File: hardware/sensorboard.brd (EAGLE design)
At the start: 21.5 x 85 mm, 29 parts, among them U3 QRE1113, U4 QRE1113, U5 QRE1113, U6 QRE1113, U7 QRE1113, U8 QRE1113, U9 QRE1113

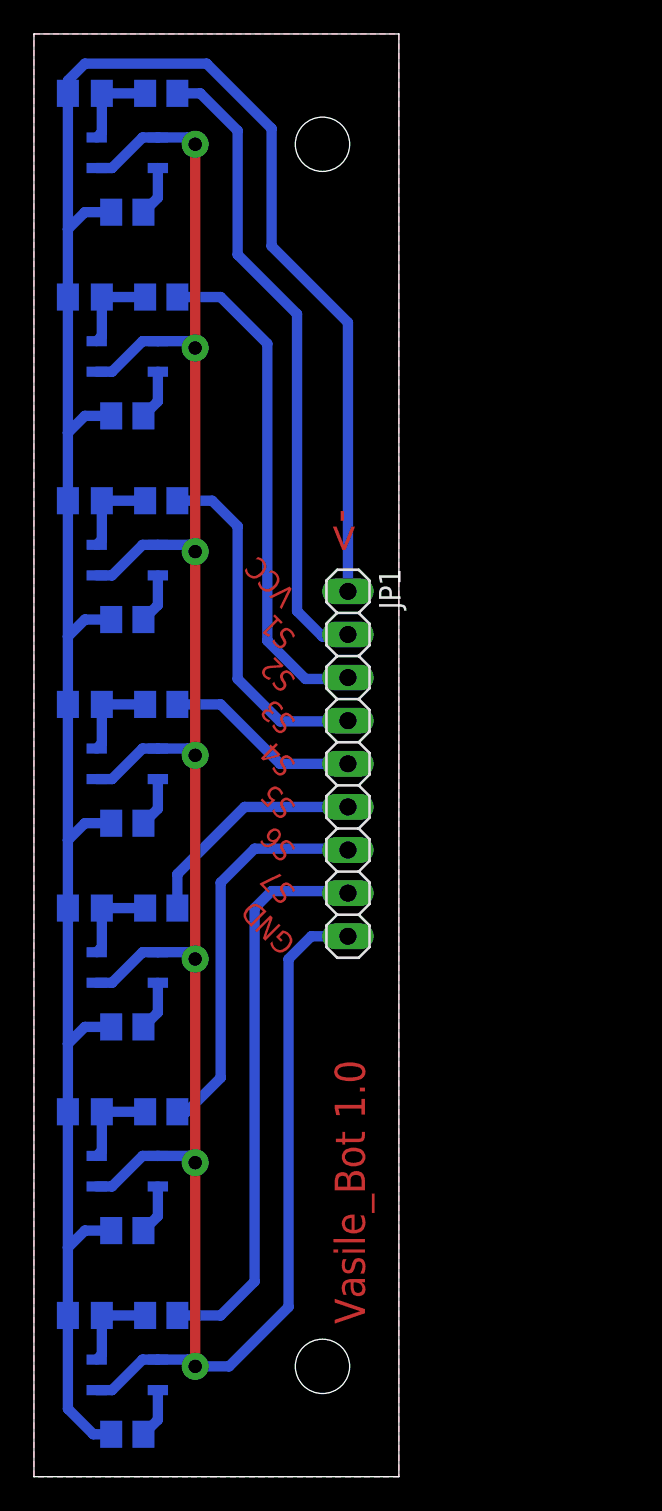
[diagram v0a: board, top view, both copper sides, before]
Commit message: Added ball caster. Added halls for ball caster. Fixed mounting halls.
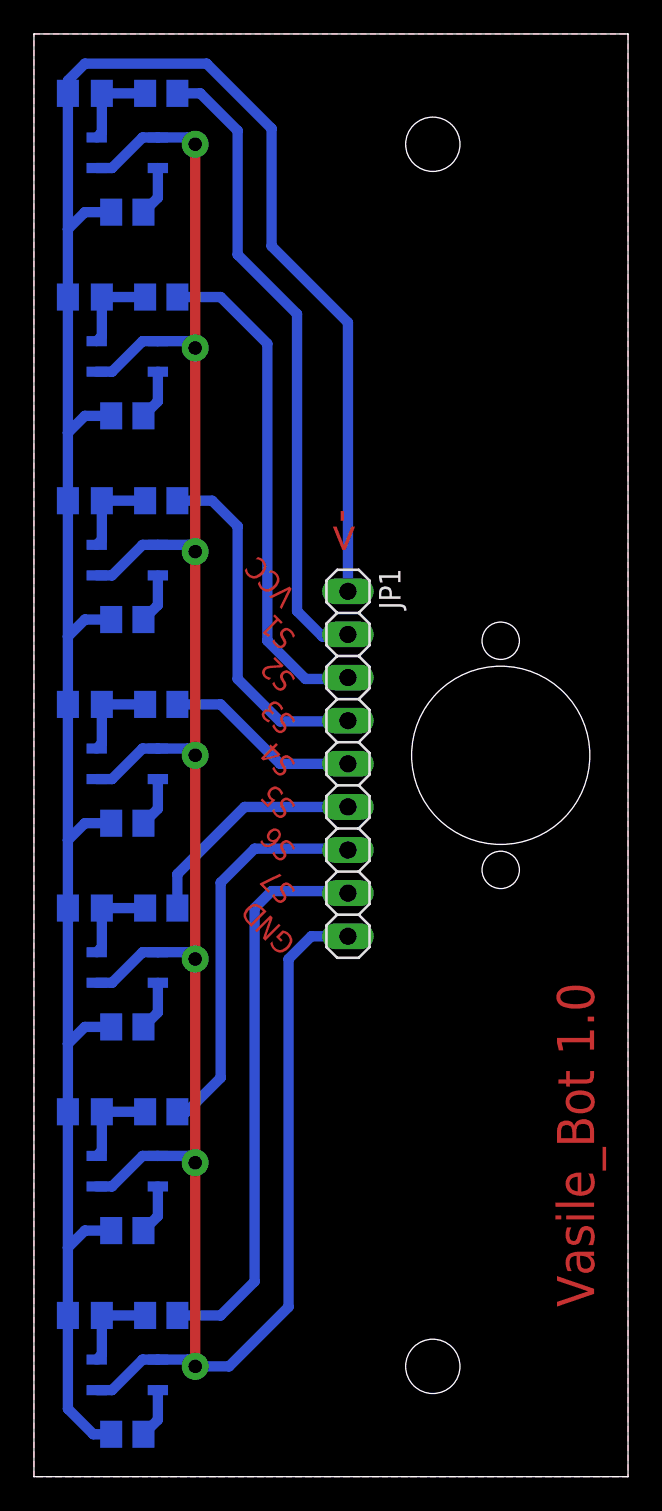
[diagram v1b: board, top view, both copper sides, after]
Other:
- board size 21.5 x 85 mm -> 35 x 85 mm
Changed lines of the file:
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@@
 <board>
 <plain>
-<wire x1="0" y1="0" x2="21.5" y2="0" width="0" layer="20"/>
-<wire x1="21.5" y1="0" x2="21.5" y2="85" width="0" layer="20"/>
-<wire x1="21.5" y1="85" x2="0" y2="85" width="0" layer="20"/>
+<wire x1="0" y1="0" x2="35" y2="0" width="0" layer="20"/>
+<wire x1="35" y1="0" x2="35" y2="85" width="0" layer="20"/>
+<wire x1="35" y1="85" x2="0" y2="85" width="0" layer="20"/>
 <wire x1="0" y1="85" x2="0" y2="0" width="0" layer="20"/>
 <text x="15.5" y="52" size="1.27" layer="1" font="vector" ratio="20" rot="SR135">VCC</text>
@@
 <text x="15.5" y="34.5" size="1.27" layer="1" font="vector" ratio="20" rot="SR135">S7</text>
 <text x="15.5" y="31.5" size="1.27" layer="1" font="vector" ratio="20" rot="SR135">GND</text>
-<text x="19.5" y="9" size="1.778" layer="1" font="vector" ratio="20" rot="R90">Vasile_Bot 1.0</text>
+<text x="33" y="10" size="2.1844" layer="1" font="vector" ratio="20" rot="R90">Vasile_Bot 1.0</text>
 <dimension x1="0" y1="85" x2="0" y2="0" x3="-4" y3="42.5" textsize="1.778" textratio="20" layer="20"/>
-<hole x="17" y="78.5" drill="3.2"/>
-<hole x="17" y="6.5" drill="3.2"/>
-<dimension x1="0" y1="85" x2="21.5" y2="85" x3="10.75" y3="89.5" textsize="1.778" textratio="20" layer="20"/>
+<hole x="23.5" y="78.5" drill="3.2"/>
+<hole x="23.5" y="6.5" drill="3.2"/>
 <text x="17.5" y="57" size="1.778" layer="1" font="vector" ratio="20" rot="SR270">-&gt;</text>
+<dimension x1="0" y1="85" x2="35" y2="85" x3="17.5" y3="94.5" textsize="1.778" textratio="20" layer="20"/>
+<hole x="27.5" y="42.5" drill="10.5"/>
+<hole x="27.5" y="49.25" drill="2.2"/>
+<hole x="27.5" y="35.75" drill="2.2"/>
 </plain>
 <attributes>
@@
 <polygon width="0.4064" layer="1" isolate="0.6096">
 <vertex x="0" y="85"/>
-<vertex x="21.5" y="85"/>
-<vertex x="21.5" y="0"/>
+<vertex x="35" y="85"/>
+<vertex x="35" y="0"/>
 <vertex x="0" y="0"/>
 </polygon>
 <polygon width="0.4064" layer="16" isolate="0.6096">
 <vertex x="0" y="85"/>
-<vertex x="21.5" y="85"/>
-<vertex x="21.5" y="0"/>
+<vertex x="35" y="85"/>
+<vertex x="35" y="0"/>
 <vertex x="0" y="0"/>
 </polygon>
